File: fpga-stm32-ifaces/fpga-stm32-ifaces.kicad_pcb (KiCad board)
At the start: 6 copper layers, 90 x 94.5 mm, 274 parts, among them J1 0826-1G1T-23-F, J10 CORTEX_DEBUG_ETM, J11 XILINX_JTAG, J12 CONN_01X03, J2 PMOD_HOST, J3 PMOD_HOST, J4 XILINX_JTAG, J5 CONN_01X03, J6 CONN_01X03, J7 CONN_PCIE_PWR_8PIN, J8 XILINX_JTAG, J9 CONN_IBC_MGMT_DEVICE, M1 LOGO, M2 LOGO, M3 LOGO, M5 SCREWHOLE, M6 SCREWHOLE, M7 SCREWHOLE, M8 SCREWHOLE, U1 STM32H735-UFBGA176-25, U10 ECS-1612MV-250-CN, U11 STM32L431-QFN48, U12 MUN12AD03-SE, U13 MUN12AD03-SE, U14 MUN12AD03-SE, U15 MUN12AD03-SE, U16 W25Q128JV, U2 XC7S25-1FTGB196, U3 S25FL128SAGBHIA10, U4 KSZ9031RN, U5 RCLAMP0514M, U6 RCLAMP0514M, U7 ECS-1612MV-250-CN, U8 AT24MAC402, U9 ECS-1612MV-250-CN

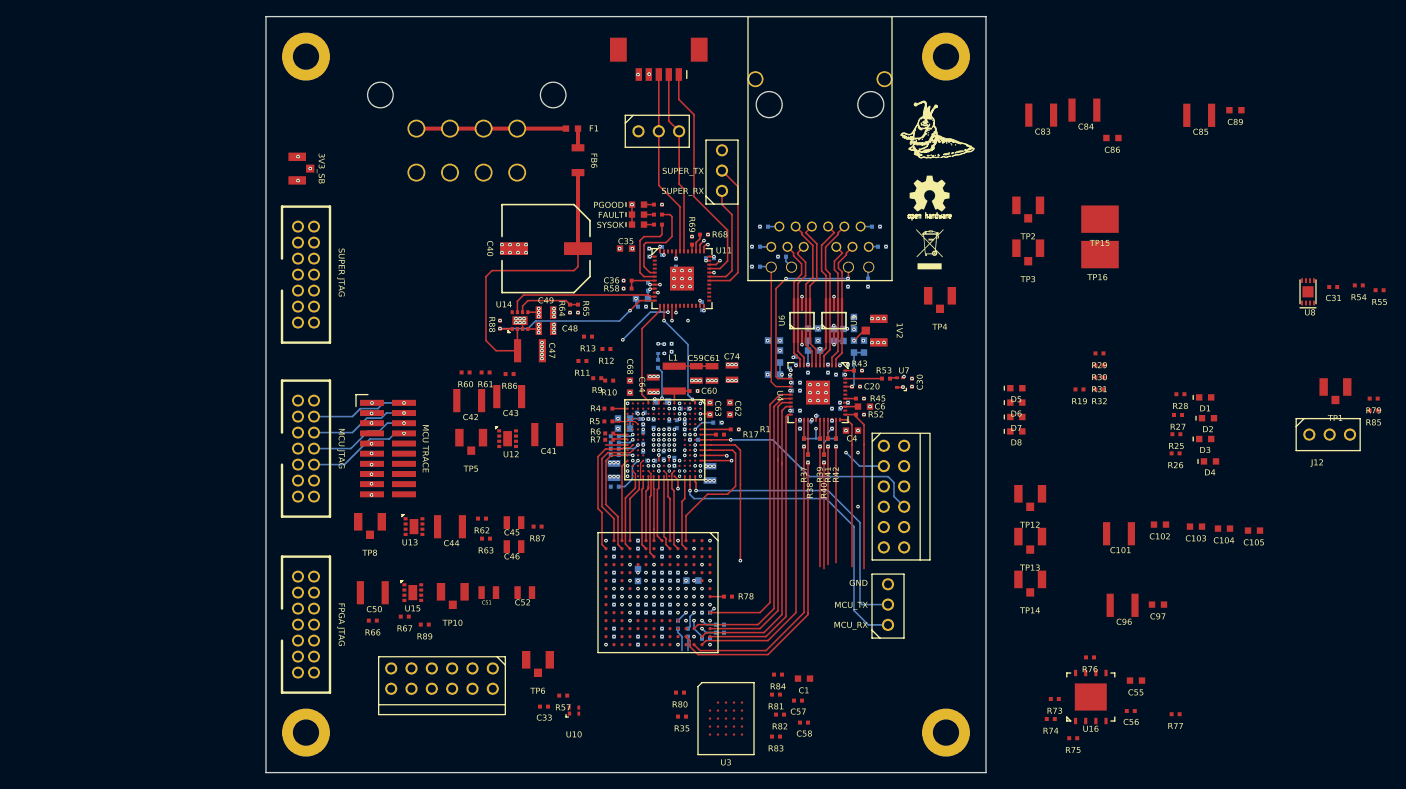
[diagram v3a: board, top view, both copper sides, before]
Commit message: Lots more routing around FPGA and MCU
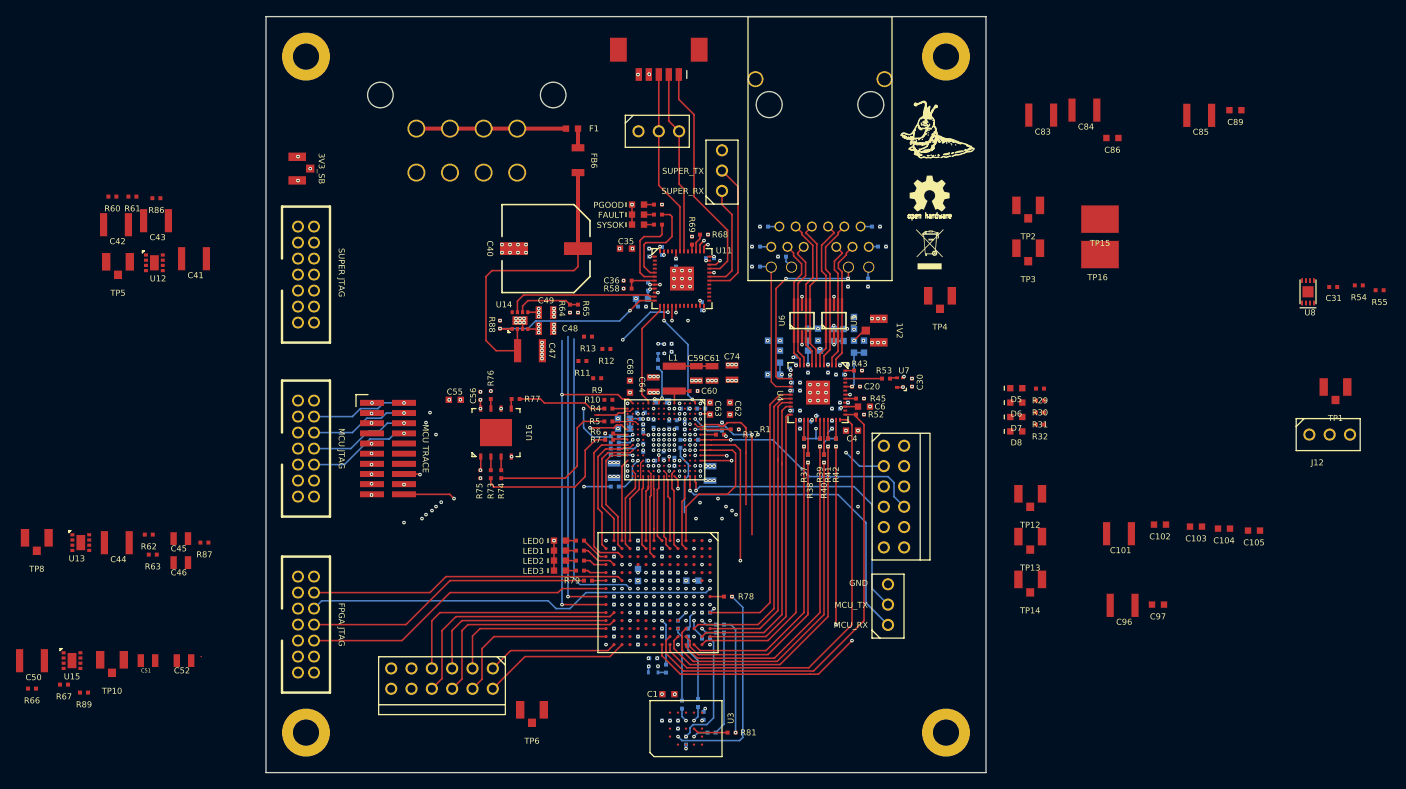
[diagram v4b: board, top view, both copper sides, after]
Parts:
- C33, C57, C58, R19, R35, R57, R80, R82, R83, R84, R85, U10: moved to B.Cu
- moved R79 100.8 mm to (68.2, 111.5)
- moved C55 92.1 mm to (51.6, 88.9), turned to 180 degrees
- moved R77 91.4 mm to (59.2, 88.8)
- moved C56 90.3 mm to (54.8, 88.4), turned to 90 degrees
- moved R85 84.1 mm to (82.4, 90.0)
- moved D2 82.7 mm to (64.8, 107.8)
- moved D1 82.6 mm to (64.8, 106.5)
- moved D4 82.4 mm to (64.8, 110.2)
- moved D3 82.1 mm to (64.8, 109.0)
- moved R76 81.8 mm to (56.1, 88.3), turned to 90 degrees
- moved U16 81.4 mm to (56.8, 93.0)
- moved R75 81.1 mm to (54.8, 98.2), turned to 90 degrees
- moved R28 78.2 mm to (67.3, 110.2), turned to 180 degrees
- moved R27 76.9 mm to (67.2, 109.0), turned to 180 degrees
- moved R73 75.9 mm to (56.1, 98.2), turned to 90 degrees
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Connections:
- U1 pad L2: /FPGA_DONE -> unconnected-(U1C-PC0-PadL2)
- U1 pad P1: unconnected-(U1A-PA0-PadP1) -> /FPGA_DONE
- U2 pad A5: /MCU/RMII_RXD0 -> /MCU/FMC_AD15
- U2 pad D12: /Ethernet/ETH_RXD1 -> /Ethernet/ETH_RXD0
- U2 pad D14: /Ethernet/ETH_RXD0 -> /Ethernet/ETH_RXD1
- U2 pad E13: unconnected-(U2C-IO_L10N_T1_D15_14-PadE13) -> /Ethernet/ETH_RX_DV
- U2 pad E4: /MCU/FPGA_LED_3 -> /MCU/FMC_A16
- U2 pad F13: unconnected-(U2C-IO_L10P_T1_D14_14-PadF13) -> /Ethernet/ETH_MDIO
- U2 pad F14: unconnected-(U2C-IO_L9N_T1_DQS_D13_14-PadF14) -> /Ethernet/ETH_MDC
- U2 pad G14: unconnected-(U2C-IO_L9P_T1_DQS_14-PadG14) -> /Ethernet/ETH_RST_N
- U2 pad H12: /Ethernet/ETH_RST_N -> unconnected-(U2C-IO_L13N_T2_MRCC_14-PadH12)
- U2 pad H13: /Ethernet/ETH_MDC -> unconnected-(U2C-IO_L14P_T2_SRCC_14-PadH13)
- U2 pad H14: /Ethernet/ETH_MDIO -> unconnected-(U2C-IO_L14N_T2_SRCC_14-PadH14)
- U2 pad L3: /MCU/FPGA_LED_2 -> /MCU/FPGA_QSPI_CS_N
- U2 pad L5: /MCU/FMC_AD7 -> /MCU/FPGA_QSPI_DQ4
- U2 pad M10: /Ethernet/FPGA_PMOD_DQ7 -> unconnected-(U2C-IO_25_14-PadM10)
- U2 pad M13: /Ethernet/ETH_RX_DV -> unconnected-(U2C-IO_L15P_T2_DQS_RDWR_B_14-PadM13)
- U2 pad M14: /Ethernet/FPGA_PMOD_DQ0 -> /Ethernet/FPGA_PMOD_DQ4
- U2 pad M3: /MCU/FPGA_QSPI_DQ4 -> /MCU/FMC_AD7
- U2 pad M4: /MCU/FMC_AD15 -> /MCU/RMII_RXD0
- U2 pad N10: /Ethernet/FPGA_PMOD_DQ3 -> /Ethernet/FPGA_PMOD_DQ7
- U2 pad N11: /Ethernet/FPGA_PMOD_DQ4 -> /Ethernet/FPGA_PMOD_DQ6
- U2 pad N14: unconnected-(U2C-IO_L21P_T3_DQS_14-PadN14) -> /Ethernet/FPGA_PMOD_DQ0
- U2 pad N4: /MCU/FPGA_QSPI_CS_N -> /MCU/FPGA_LED_1
- U2 pad P10: /Ethernet/FPGA_PMOD_DQ5 -> /Ethernet/FPGA_PMOD_DQ3
- U2 pad P11: /Ethernet/FPGA_PMOD_DQ6 -> /Ethernet/FPGA_PMOD_DQ2
- U2 pad P13: /Ethernet/FPGA_PMOD_DQ2 -> /Ethernet/FPGA_PMOD_DQ5
- U2 pad P3: /MCU/FPGA_LED_1 -> /MCU/FPGA_LED_0
- U2 pad P4: /MCU/FPGA_LED_0 -> /MCU/FPGA_LED_2
- U2 pad P5: /MCU/FMC_A16 -> /MCU/FPGA_LED_3
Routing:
- net /GND: track 713.9 -> 809.2 mm, vias 234 -> 243
- net /3V3: track 252.3 -> 333.8 mm, vias 53 -> 64
- net /Ethernet/ETH_RST_N: track 0.00 -> 59.3 mm, vias 0 -> 2
- net /MCU/MCU_JTAG_TDO: track 19.8 -> 76.4 mm, vias 2 -> 5
- net /MCU/MCU_JTAG_TCK: track 19.6 -> 75.6 mm, vias 2 -> 5
- net /MCU/TRACED2: track 0.00 -> 55.6 mm, vias 1 -> 4
- net /MCU/MCU_JTAG_TDI: track 20.2 -> 71.9 mm, vias 2 -> 5
- net /FPGA_TCK: track 0.00 -> 51.3 mm, vias 0 -> 1
- net /MCU/MCU_JTAG_TMS: track 15.9 -> 66.1 mm, vias 2 -> 4
- net /FPGA_DONE: track 0.00 -> 47.8 mm, vias 0 -> 2
- net /MCU/TRACED3: track 0.00 -> 47.0 mm, vias 1 -> 3
- net /MCU/TRACED1: track 2.55 -> 48.4 mm, vias 1 -> 4
- net /FPGA_TMS: track 0.00 -> 39.5 mm
- net /FPGA_TDI: track 0.00 -> 39.2 mm
- net /FPGA_RST_N: track 0.00 -> 37.5 mm, vias 0 -> 1
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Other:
- board text added: "LED0"
- board text added: "LED1"
- board text added: "LED2"
- board text added: "LED3"

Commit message: More FPGA power routing
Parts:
- R66, R67: moved to B.Cu
- moved TP8 65.6 mm to (62.5, 124.0), turned to 180 degrees
- moved TP10 59.3 mm to (68.0, 124.0), turned to 180 degrees
- moved R66 52.9 mm to (49.3, 109.3), turned to 90 degrees
- moved U13 50.9 mm to (55.7, 109.3)
- moved R67 48.0 mm to (48.1, 108.8), turned to 180 degrees
- moved R62 46.1 mm to (59.2, 110.2), turned to 90 degrees
- moved C50 45.8 mm to (42.8, 108.8), turned to 180 degrees
- moved U15 45.6 mm to (47.5, 108.5)
- moved R63 45.4 mm to (59.2, 108.5), turned to 90 degrees
- moved R89 44.3 mm to (45.5, 107.0), turned to 90 degrees
- moved C44 42.8 mm to (52.0, 110.5), turned to -90 degrees
- moved C46 40.3 mm to (57.5, 112.4), turned to -90 degrees
- moved C45 38.4 mm to (55.2, 112.4), turned to -90 degrees
- moved C51 34.4 mm to (46.2, 111.8), turned to -90 degrees
- moved R87 33.2 mm to (53.5, 107.0), turned to 90 degrees
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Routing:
- net /GND: track 809.2 -> 905.2 mm, vias 243 -> 296
- net /12V0: track 39.1 -> 106.1 mm
- net /MCU/TRACECLK: track 0.00 -> 53.1 mm, vias 0 -> 4
- net /MCU/TRACED0: track 0.00 -> 44.2 mm, vias 0 -> 3
- net /MCU_RST_N: track 13.5 -> 56.3 mm, vias 0 -> 4
- net /Power supply/1V0: track 28.6 -> 69.9 mm, vias 13 -> 21
- net /Power supply/1V8: track 23.4 -> 58.4 mm, vias 6 -> 14
- net /Power supply/1V0_PGOOD: track 0.00 -> 29.0 mm, vias 0 -> 1
- net /Power supply/1V8_EN: track 0.00 -> 28.3 mm, vias 0 -> 1
- net /Power supply/1V0_EN: track 0.00 -> 24.0 mm, vias 0 -> 1
- net /Power supply/1V8_PGOOD: track 0.00 -> 23.3 mm, vias 0 -> 1
- net /MCU/TRACED3: track 47.0 -> 52.2 mm
- net Net-(U13-FB): track 0.00 -> 3.31 mm
- net /MCU/TRACED2: track 55.6 -> 52.8 mm
- net /FPGA_TMS: track 39.5 -> 42.2 mm
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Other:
- board text added: "12V0"
- board text added: "1V0"
- board text added: "1V8"
- board text added: "FPGA PMOD"
- board text added: "MCU PMOD"

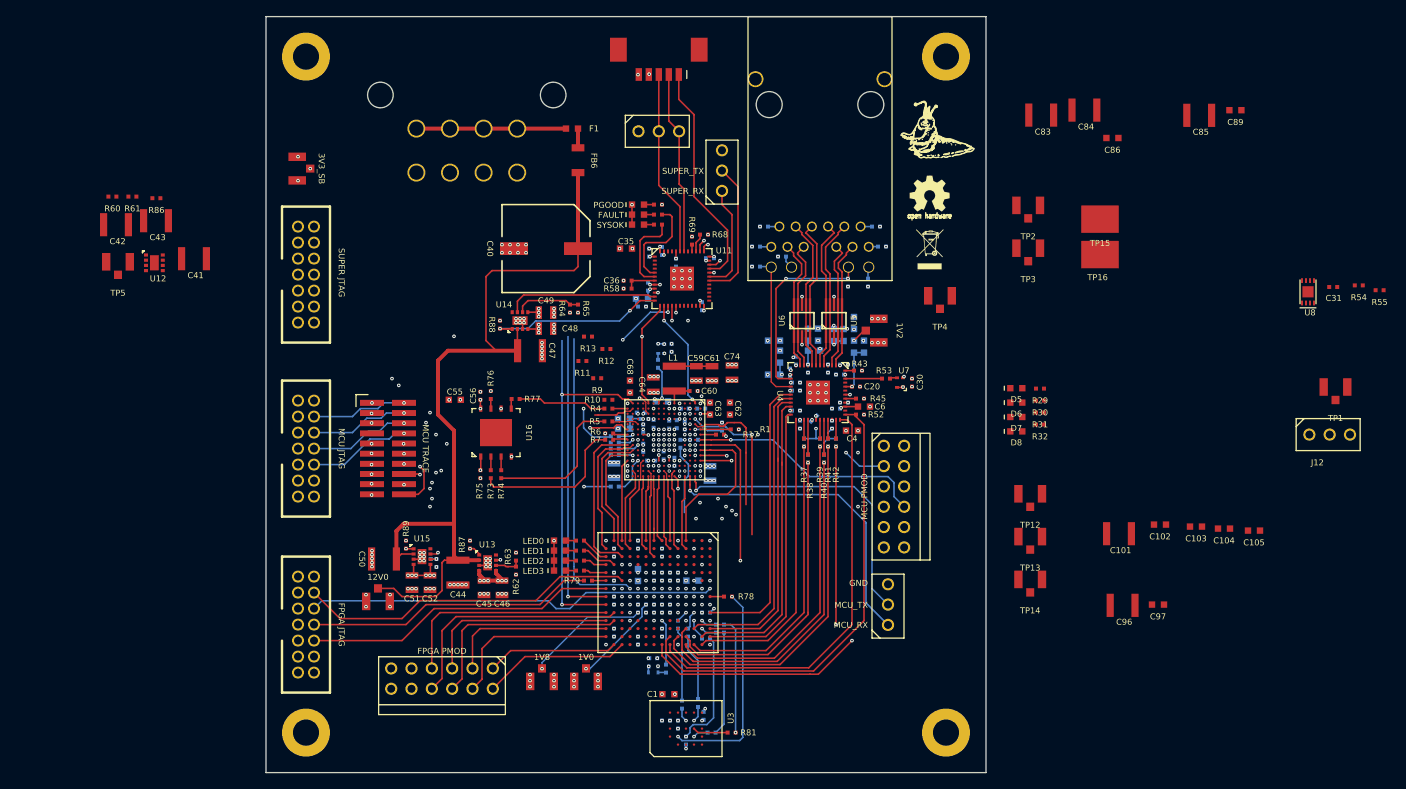
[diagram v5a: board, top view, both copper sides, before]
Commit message: Continued fpga-stm32-ifaces layout
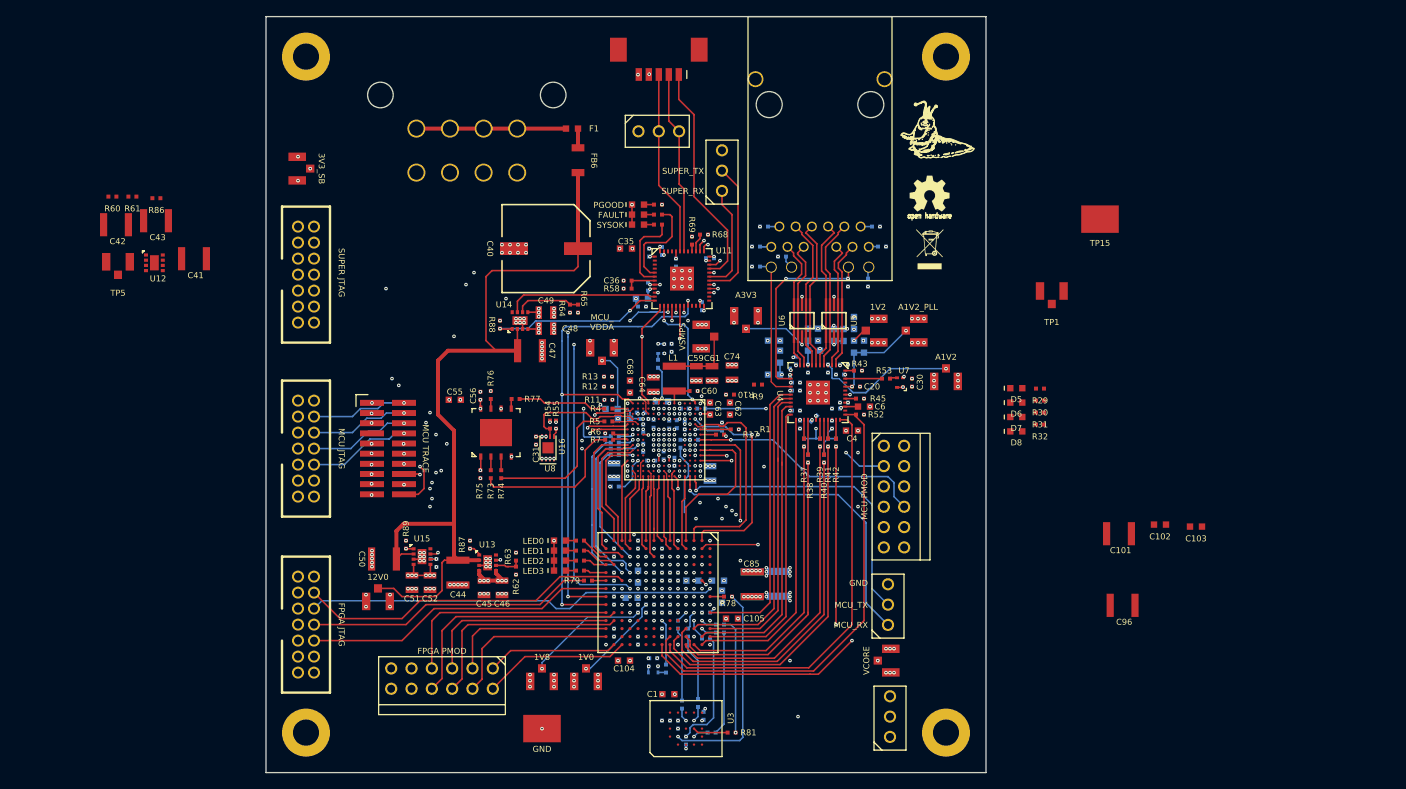
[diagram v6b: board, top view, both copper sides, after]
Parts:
- C83, C84, C86, C89, C97: moved to B.Cu
- moved R55 104.3 mm to (64.2, 92.0), turned to 90 degrees
- moved R54 102.6 mm to (63.5, 92.0), turned to 90 degrees
- moved C31 101.5 mm to (61.8, 94.0), turned to -90 degrees
- moved C89 97.0 mm to (73.7, 113.7), turned to 180 degrees
- moved U8 97.0 mm to (63.2, 94.9)
- moved TP16 91.5 mm to (62.5, 130.0)
- moved C85 81.0 mm to (88.8, 112.0), turned to -90 degrees
- moved C104 76.8 mm to (72.8, 121.5)
- moved C86 74.1 mm to (84.5, 111.5), turned to 180 degrees
- moved C84 72.4 mm to (88.8, 112.0), turned to -90 degrees
- moved C83 67.2 mm to (92.0, 111.9), turned to -90 degrees
- moved C105 66.2 mm to (86.2, 116.2)
- moved J12 65.3 mm to (106.0, 128.5), turned to 90 degrees
- moved TP14 60.9 mm to (70.0, 82.5)
- moved C97 54.5 mm to (85.0, 113.5), turned to -90 degrees
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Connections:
- U11 pad 18: /Power supply/1V8_EN -> /FPGA_RST_N
- U11 pad 19: /FPGA_RST_N -> /FPGA_INIT
- U11 pad 25: /Power supply/1V0_PGOOD -> /Power supply/3V3_EN
- U11 pad 26: /Power supply/1V0_EN -> /Power supply/3V3_PGOOD
- U11 pad 27: /Power supply/3V3_PGOOD -> /Power supply/1V8_PGOOD
- U11 pad 28: /Power supply/1V8_PGOOD -> /Power supply/1V0_EN
- U11 pad 29: /Power supply/3V3_EN -> /Power supply/1V0_PGOOD
- U11 pad 32: /FPGA_INIT -> /Power supply/1V8_EN
- U2 pad A2: /MCU/FMC_NBL0 -> /MCU/FMC_NWE
- U2 pad A3: /MCU/FPGA_QSPI_DQS -> /MCU/FPGA_QSPI_CS_N
- U2 pad A4: /MCU/FMC_NWAIT -> /MCU/FMC_NOE
- U2 pad A5: /MCU/FMC_AD15 -> /MCU/FPGA_QSPI_DQ6
- U2 pad B1: /MCU/FMC_AD1 -> /MCU/FMC_NBL0
- U2 pad B2: /MCU/FMC_AD9 -> /MCU/FPGA_QSPI_DQ7
- U2 pad B3: /MCU/FMC_NL_NADV -> /MCU/FPGA_QSPI_DQ0
- U2 pad B6: /MCU/FPGA_QSPI_DQ6 -> /MCU/FPGA_QSPI_DQ3
- U2 pad C1: /MCU/FPGA_QSPI_DQ0 -> /MCU/FMC_NL_NADV
- U2 pad C3: /MCU/FMC_NWE -> /MCU/FMC_NWAIT
- U2 pad C4: /MCU/FPGA_QSPI_DQ7 -> /MCU/FPGA_QSPI_DQ1
- U2 pad C5: /MCU/FMC_AD2 -> /MCU/FPGA_QSPI_DQ2
- U2 pad D3: /MCU/FMC_NOE -> /MCU/FMC_AD2
- U2 pad D4: /MCU/FMC_AD5 -> /MCU/FMC_AD1
- U2 pad F3: /MCU/FPGA_QSPI_DQ5 -> /MCU/FMC_AD14
- U2 pad F4: /MCU/RMII_CRS_DV -> /MCU/FMC_AD15
- U2 pad J3: /MCU/FPGA_QSPI_DQ2 -> /MCU/FMC_AD5
- U2 pad J4: /MCU/FPGA_QSPI_DQ3 -> /MCU/RMII_RXD1
- U2 pad K3: /MCU/FPGA_QSPI_DQ1 -> /MCU/FMC_AD9
- U2 pad K4: /MCU/RMII_RXD1 -> /MCU/RMII_CRS_DV
- U2 pad L3: /MCU/FPGA_QSPI_CS_N -> /MCU/FPGA_QSPI_DQS
- U2 pad L5: /MCU/FPGA_QSPI_DQ4 -> /MCU/FPGA_QSPI_DQ5
- U2 pad M5: /MCU/FMC_AD14 -> /MCU/FPGA_QSPI_DQ4
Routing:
- net /GND: track 905.2 -> 993.4 mm, vias 296 -> 347
- net /3V3: track 333.8 -> 413.4 mm, vias 64 -> 71
- net Net-(J12-P2): track 0.00 -> 59.3 mm, vias 0 -> 2
- net /Power supply/1V0_EN: track 24.0 -> 77.9 mm, vias 1 -> 3
- net /MCU/FPGA_QSPI_DQ3: track 0.00 -> 46.9 mm, vias 0 -> 2
- net /Power support/VCORE: track 22.4 -> 65.3 mm, vias 9 -> 12
- net /MCU/FPGA_QSPI_DQ2: track 0.00 -> 41.9 mm, vias 0 -> 2
- net /Power supply/1V0_PGOOD: track 29.0 -> 68.0 mm, vias 1 -> 3
- net /Power supply/1V8_EN: track 28.3 -> 67.0 mm, vias 1 -> 3
- net /Power supply/1V8_PGOOD: track 23.3 -> 61.0 mm, vias 1 -> 3
- net /MCU/RMII_REF_CLK: track 5.08 -> 37.4 mm, vias 0 -> 2
- net /MCU/RMII_CRS_DV: track 0.00 -> 31.8 mm, vias 0 -> 3
- net /MCU/FMC_AD9: track 0.00 -> 27.9 mm, vias 0 -> 3
- net /MCU/FPGA_QSPI_SCK: track 0.00 -> 24.5 mm, vias 0 -> 3
- net /Ethernet/A1V2: track 5.70 -> 27.3 mm, vias 2 -> 3
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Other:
- board text added: "A1V2"
- board text added: "A1V2_PLL"
- board text added: "A3V3"
- board text added: "MCU_ VDDA"
- board text added: "VCORE"
- board text added: "VSMPS"
